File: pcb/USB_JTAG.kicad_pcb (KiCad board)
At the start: 4 copper layers, 33.5 x 15 mm, 29 parts, among them J1 USBC_China16, J2 Conn_01x08_Male, U1 Q6CVQ, U2 JPPQ9, U3 26HRB, U4 6MMF7, U5 6MMF7, U6 6MMF7, U8 6MMF7

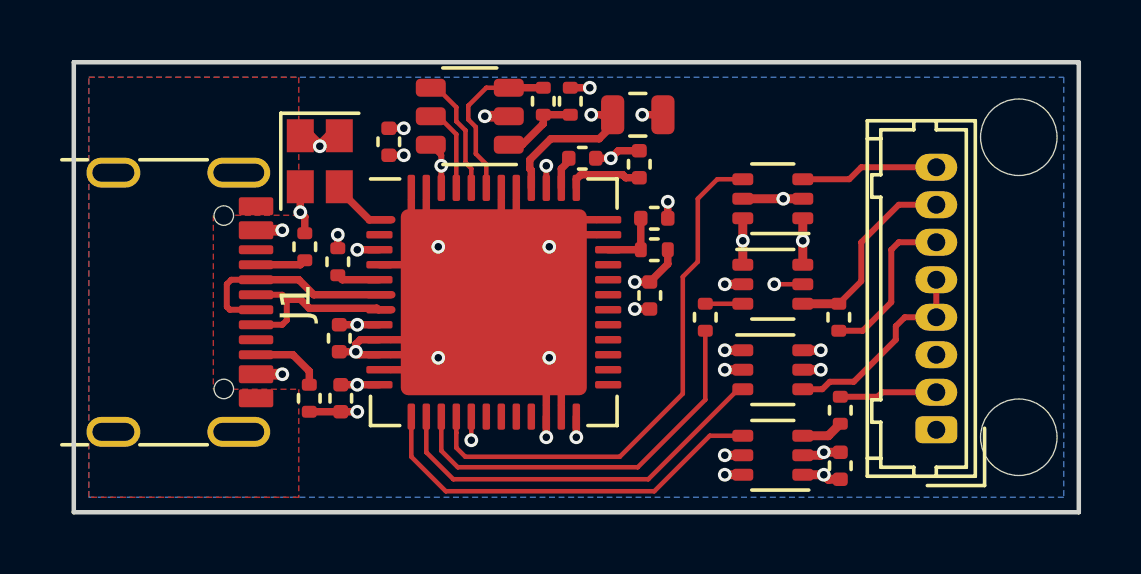
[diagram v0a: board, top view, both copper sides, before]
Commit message: fix TDI/TDO swap closes #2
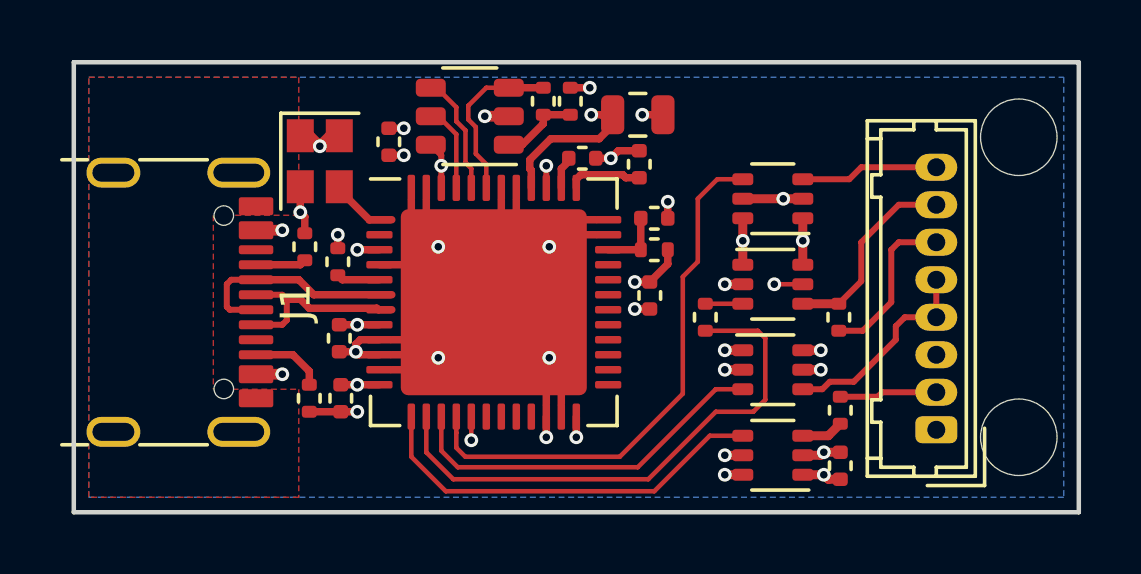
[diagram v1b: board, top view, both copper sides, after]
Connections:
- net /TDO2 renamed /TDI2
- J2 pad 4: /TDI -> /TDO
- J2 pad 5: /TDI -> /TDO
- J2 pad 7: /TDO -> /TDI
- R8 pad 2: /TDO -> /TDI
- R9 pad 2: /TDO1 -> /TDI1
- U4 pad 3: /TDI1 -> /TDO1
- U4 pad 4: /TDI -> /TDO
- U8 pad 4: /TDO -> /TDI
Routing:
- net /TDI1: track 13.4 -> 18.1 mm
- net /TDO1: track 13.4 -> 12.5 mm
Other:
- board text added: "Harmon Instruments USB to JTAG Rev 5.1"
- board text removed: "Harmon Instruments USB to JTAG Rev 5"

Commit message: Fix net labels closes #3
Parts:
- J1: value USBC_China16 -> CGH8B; footprint kicad_pcb:USB_C_Receptacle_China_16pin -> kicad_pcb:USB_C_Receptacle_HRO_TYPE-C-31-M-12
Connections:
- net /TDI2 renamed /TDO2
- J2 pad 4: /TDO -> /TDI
- J2 pad 5: /TDO -> /TDI
- J2 pad 7: /TDI -> /TDO
- R8 pad 2: /TDI -> /TDO
- R9 pad 2: /TDI1 -> /TDO1
- U3 pad 14: /TDI1 -> /TDO1
- U3 pad 15: /TDO1 -> /TDI1
- U4 pad 3: /TDO1 -> /TDI1
- U4 pad 4: /TDO -> /TDI
- U8 pad 4: /TDI -> /TDO
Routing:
- net /TDO1: track 12.5 -> 18.1 mm
- net /TDI1: track 18.1 -> 12.5 mm
